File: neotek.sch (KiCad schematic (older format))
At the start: 18 parts, among them P1 USB_OTG, U1 STM32F103C4, U2 MIC5219-3.3, Y1 Crystal

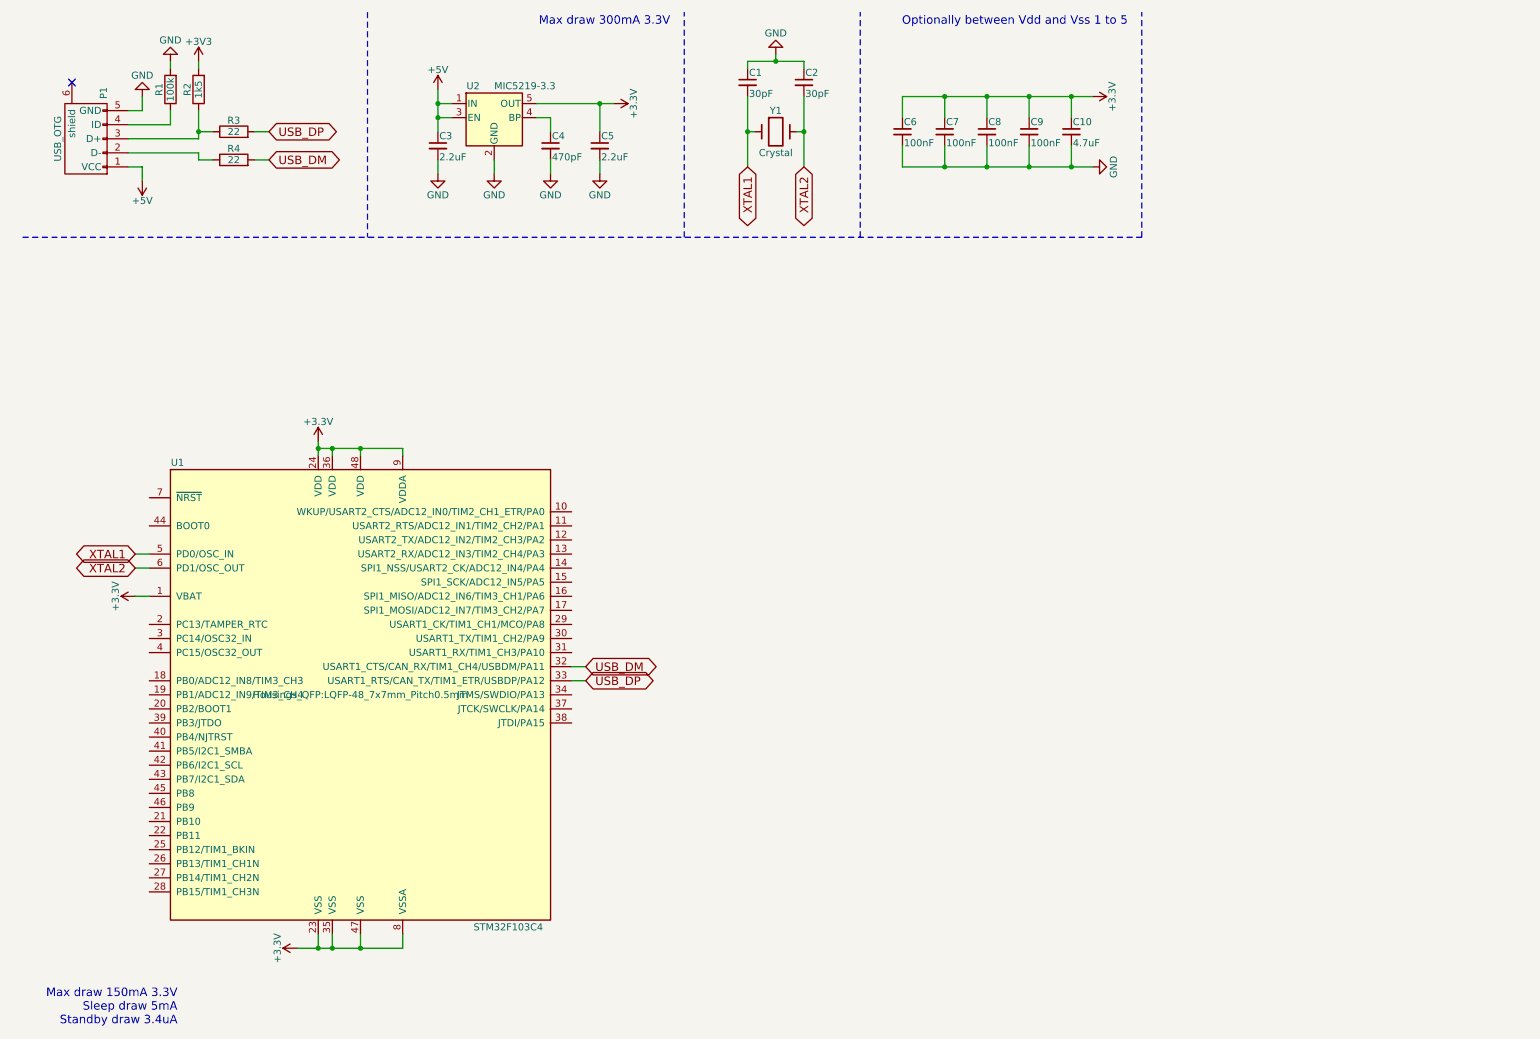
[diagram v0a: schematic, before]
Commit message: Added headers; made footprint & layout stub
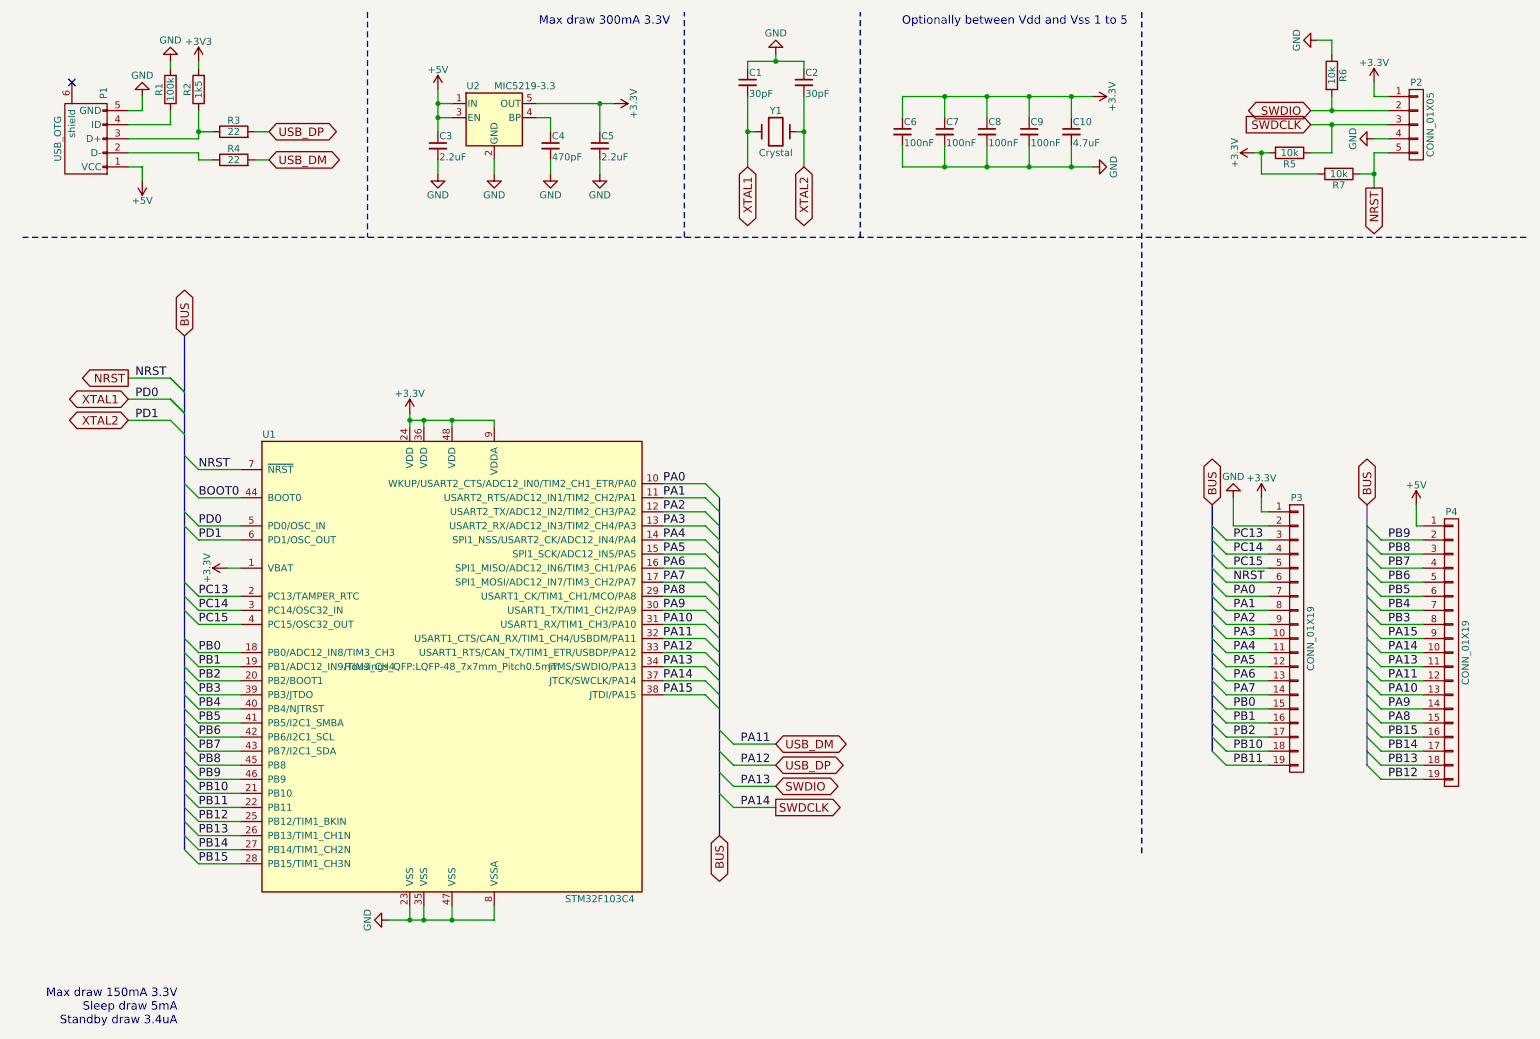
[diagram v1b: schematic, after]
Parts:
- added P2: CONN_01X05, Connectors_Hirose:Hirose_DF13-05P-1.25DS_05x1.25mm_Angled, symbol CONN_01X05
- added P3, P4: CONN_01X19, Pin_Headers:Pin_Header_Straight_1x19, symbol CONN_01X19
- added R5, R6, R7: 10k, Resistors_SMD:R_0603_HandSoldering, symbol R
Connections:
- net +3V3: now also P2.1 (P1), P3.1 (P1), R5.2, R7.2; no longer U1.23 (VSS), U1.35 (VSS), U1.47 (VSS), U1.8 (VSSA)
- net +5V: now also P4.1 (P1)
- net GND: now also U1.23 (VSS), U1.35 (VSS), U1.47 (VSS), U1.8 (VSSA), P2.4 (P4), P3.2 (P2), R6.1
- net USB_DM: now also P4.12 (P12)
- net PA0: now reaches U1.10 (WKUP/USART2_CTS/ADC12_IN0/TIM2_CH1_ETR/PA0)
- net PA0: now also P3.7 (P7)
- net PA1: now reaches U1.11 (USART2_RTS/ADC12_IN1/TIM2_CH2/PA1)
- net PA1: now also P3.8 (P8)
- net PA2: now reaches U1.12 (USART2_TX/ADC12_IN2/TIM2_CH3/PA2)
- net PA2: now also P3.9 (P9)
- net PA3: now reaches U1.13 (USART2_RX/ADC12_IN3/TIM2_CH4/PA3)
- net PA3: now also P3.10 (P10)
- net PA4: now reaches U1.14 (SPI1_NSS/USART2_CK/ADC12_IN4/PA4)
- net PA4: now also P3.11 (P11)
- net PA5: now reaches U1.15 (SPI1_SCK/ADC12_IN5/PA5)
- net PA5: now also P3.12 (P12)
- net PA6: now reaches U1.16 (SPI1_MISO/ADC12_IN6/TIM3_CH1/PA6)
- net PA6: now also P3.13 (P13)
- net PA7: now reaches U1.17 (SPI1_MOSI/ADC12_IN7/TIM3_CH2/PA7)
- net PA7: now also P3.14 (P14)
- net PB0: now reaches U1.18 (PB0/ADC12_IN8/TIM3_CH3)
- net PB0: now also P3.15 (P15)
- net PB1: now reaches U1.19 (PB1/ADC12_IN9/TIM3_CH4)
- net PB1: now also P3.16 (P16)
- net PC13: now reaches U1.2 (PC13/TAMPER_RTC)
- net PC13: now also P3.3 (P3)
- net PB2: now reaches U1.20 (PB2/BOOT1)
- net PB2: now also P3.17 (P17)
- net PB10: now reaches U1.21 (PB10)
- net PB10: now also P3.18 (P18)
- net PB11: now reaches U1.22 (PB11)
- net PB11: now also P3.19 (P19)
- net PB12: now reaches U1.25 (PB12/TIM1_BKIN)
- net PB12: now also P4.19 (P19)
- net PB13: now reaches U1.26 (PB13/TIM1_CH1N)
- net PB13: now also P4.18 (P18)
- net PB14: now reaches U1.27 (PB14/TIM1_CH2N)
- net PB14: now also P4.17 (P17)
- net PB15: now reaches U1.28 (PB15/TIM1_CH3N)
- net PB15: now also P4.16 (P16)
- net PA8: now reaches U1.29 (USART1_CK/TIM1_CH1/MCO/PA8)
- net PA8: now also P4.15 (P15)
- net PC14: now reaches U1.3 (PC14/OSC32_IN)
- net PC14: now also P3.4 (P4)
- net PA9: now reaches U1.30 (USART1_TX/TIM1_CH2/PA9)
- net PA9: now also P4.14 (P14)
- net PA10: now reaches U1.31 (USART1_RX/TIM1_CH3/PA10)
- net PA10: now also P4.13 (P13)
- net SWDIO: now reaches U1.34 (JTMS/SWDIO/PA13)
- net SWDIO: now also P2.2 (P2), P4.11 (P11), R6.2
- net SWDCLK: now reaches U1.37 (JTCK/SWCLK/PA14)
- net SWDCLK: now also P2.3 (P3), P4.10 (P10), R5.1
- net PA15: now reaches U1.38 (JTDI/PA15)
- net PA15: now also P4.9 (P9)
- net PB3: now reaches U1.39 (PB3/JTDO)
- net PB3: now also P4.8 (P8)
- net PC15: now reaches U1.4 (PC15/OSC32_OUT)
- net PC15: now also P3.5 (P5)
- net PB4: now reaches U1.40 (PB4/NJTRST)
- net PB4: now also P4.7 (P7)
- net PB5: now reaches U1.41 (PB5/I2C1_SMBA)
- net PB5: now also P4.6 (P6)
- net PB6: now reaches U1.42 (PB6/I2C1_SCL)
- net PB6: now also P4.5 (P5)
- net PB7: now reaches U1.43 (PB7/I2C1_SDA)
- net PB7: now also P4.4 (P4)
- net BOOT0: now reaches U1.44 (BOOT0)
- net PB8: now reaches U1.45 (PB8)
- net PB8: now also P4.3 (P3)
- net PB9: now reaches U1.46 (PB9)
- net PB9: now also P4.2 (P2)
- net NRST: now reaches U1.7 (~NRST)
- net NRST: now also P2.5 (P5), P3.6 (P6), R7.1
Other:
- moved on the sheet: U1

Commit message: wip
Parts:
- P1: footprint Connect:USB_Micro-B -> Connect:USB_Micro-B_10103594-0001LF
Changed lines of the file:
@@
 F 0 "P1" H 1275 1275 50  0000 C CNN
 F 1 "USB_OTG" H 950 1600 50  0000 C CNN
-F 2 "Connect:USB_Micro-B" V 900 1300 50  0001 C CNN
+F 2 "Connect:USB_Micro-B_10103594-0001LF" V 900 1300 50  0001 C CNN
 F 3 "" V 900 1300 50  0000 C CNN
 	1    950  1400
@@
 Connection ~ 3550 6950
 $Comp
-L +3.3V #PWR07
+L +3.3V #PWR06
 U 1 1 5A6E46B8
 P 3250 3350
-F 0 "#PWR07" H 3250 3200 50  0001 C CNN
+F 0 "#PWR06" H 3250 3200 50  0001 C CNN
 F 1 "+3.3V" H 3250 3490 50  0000 C CNN
 F 2 "" H 3250 3350 50  0000 C CNN
@@
 Connection ~ 3550 3400
 $Comp
-L +3.3V #PWR08
+L +3.3V #PWR07
 U 1 1 5A6E4886
 P 1950 4450
-F 0 "#PWR08" H 1950 4300 50  0001 C CNN
+F 0 "#PWR07" H 1950 4300 50  0001 C CNN
 F 1 "+3.3V" H 1950 4590 50  0000 C CNN
 F 2 "" H 1950 4450 50  0000 C CNN
@@
 $EndComp
 $Comp
-L +5V #PWR09
+L +5V #PWR08
 U 1 1 5A6E4C63
 P 3450 1050
-F 0 "#PWR09" H 3450 900 50  0001 C CNN
+F 0 "#PWR08" H 3450 900 50  0001 C CNN
 F 1 "+5V" H 3450 1190 50  0000 C CNN
 F 2 "" H 3450 1050 50  0000 C CNN
@@
 	3450 1150 3550 1150
 $Comp
-L GND #PWR010
+L GND #PWR09
 U 1 1 5A6E4D61
 P 3850 1650
-F 0 "#PWR010" H 3850 1400 50  0001 C CNN
+F 0 "#PWR09" H 3850 1400 50  0001 C CNN
 F 1 "GND" H 3850 1500 50  0000 C CNN
 F 2 "" H 3850 1650 50  0000 C CNN
@@
 $EndComp
 $Comp
-L GND #PWR011
+L GND #PWR010
 U 1 1 5A6E4E0C
 P 4250 1650
-F 0 "#PWR011" H 4250 1400 50  0001 C CNN
+F 0 "#PWR010" H 4250 1400 50  0001 C CNN
 F 1 "GND" H 4250 1500 50  0000 C CNN
 F 2 "" H 4250 1650 50  0000 C CNN
@@
 $EndComp
 $Comp
-L GND #PWR012
+L GND #PWR011
 U 1 1 5A6E50E3
 P 4600 1650
-F 0 "#PWR012" H 4600 1400 50  0001 C CNN
+F 0 "#PWR011" H 4600 1400 50  0001 C CNN
 F 1 "GND" H 4600 1500 50  0000 C CNN
 F 2 "" H 4600 1650 50  0000 C CNN
@@
 Connection ~ 3450 1250
 $Comp
-L GND #PWR013
+L GND #PWR012
 U 1 1 5A6E5BDB
 P 3450 1650
-F 0 "#PWR013" H 3450 1400 50  0001 C CNN
+F 0 "#PWR012" H 3450 1400 50  0001 C CNN
 F 1 "GND" H 3450 1500 50  0000 C CNN
 F 2 "" H 3450 1650 50  0000 C CNN
@@
 $EndComp
 $Comp
-L GND #PWR014
+L GND #PWR013
 U 1 1 5A6E6C90
 P 8100 1600
-F 0 "#PWR014" H 8100 1350 50  0001 C CNN
+F 0 "#PWR013" H 8100 1350 50  0001 C CNN
 F 1 "GND" H 8100 1450 50  0000 C CNN
 F 2 "" H 8100 1600 50  0000 C CNN
@@
 $EndComp
 $Comp
-L +3.3V #PWR015
+L +3.3V #PWR014
 U 1 1 5A6E6E8E
 P 4700 1150
-F 0 "#PWR015" H 4700 1000 50  0001 C CNN
+F 0 "#PWR014" H 4700 1000 50  0001 C CNN
 F 1 "+3.3V" H 4700 1290 50  0000 C CNN
 F 2 "" H 4700 1150 50  0000 C CNN
@@
 $EndComp
 $Comp
-L +3.3V #PWR016
+L +3.3V #PWR015
 U 1 1 5A6E6F17
 P 8100 1100
-F 0 "#PWR016" H 8100 950 50  0001 C CNN
+F 0 "#PWR015" H 8100 950 50  0001 C CNN
 F 1 "+3.3V" H 8100 1240 50  0000 C CNN
 F 2 "" H 8100 1100 50  0000 C CNN
@@
 	8450 500  8450 6500
 $Comp
-L +3.3V #PWR017
+L +3.3V #PWR016
 U 1 1 5A6F8D21
 P 10100 1000
-F 0 "#PWR017" H 10100 850 50  0001 C CNN
+F 0 "#PWR016" H 10100 850 50  0001 C CNN
 F 1 "+3.3V" H 10100 1140 50  0000 C CNN
 F 2 "" H 10100 1000 50  0000 C CNN
@@
 SWDIO
 $Comp
-L GND #PWR018
+L GND #PWR017
 U 1 1 5A6F91D4
 P 9700 700
-F 0 "#PWR018" H 9700 450 50  0001 C CNN
+F 0 "#PWR017" H 9700 450 50  0001 C CNN
 F 1 "GND" H 9700 550 50  0000 C CNN
 F 2 "" H 9700 700 50  0000 C CNN
@@
 Connection ~ 9800 1200
 $Comp
-L GND #PWR019
+L GND #PWR018
 U 1 1 5A6F96FC
 P 10100 1400
-F 0 "#PWR019" H 10100 1150 50  0001 C CNN
+F 0 "#PWR018" H 10100 1150 50  0001 C CNN
 F 1 "GND" H 10100 1250 50  0000 C CNN
 F 2 "" H 10100 1400 50  0000 C CNN
@@
 Connection ~ 9800 1300
 $Comp
-L +3.3V #PWR020
+L +3.3V #PWR019
 U 1 1 5A6F9C7A
 P 9250 1500
-F 0 "#PWR020" H 9250 1350 50  0001 C CNN
+F 0 "#PWR019" H 9250 1350 50  0001 C CNN
 F 1 "+3.3V" H 9250 1640 50  0000 C CNN
 F 2 "" H 9250 1500 50  0000 C CNN
@@
 NRST
 $Comp
-L +3.3V #PWR021
+L +3.3V #PWR020
 U 1 1 5A708845
 P 9300 3950
-F 0 "#PWR021" H 9300 3800 50  0001 C CNN
+F 0 "#PWR020" H 9300 3800 50  0001 C CNN
 F 1 "+3.3V" H 9300 4090 50  0000 C CNN
 F 2 "" H 9300 3950 50  0000 C CNN
@@
 $EndComp
 $Comp
-L GND #PWR022
+L GND #PWR021
 U 1 1 5A708A18
 P 9100 3950
-F 0 "#PWR022" H 9100 3700 50  0001 C CNN
+F 0 "#PWR021" H 9100 3700 50  0001 C CNN
 F 1 "GND" H 9100 3800 50  0000 C CNN
 F 2 "" H 9100 3950 50  0000 C CNN
@@
 $EndComp
 $Comp
-L +5V #PWR023
+L +5V #PWR022
 U 1 1 5A708B9F
 P 10400 4000
-F 0 "#PWR023" H 10400 3850 50  0001 C CNN
+F 0 "#PWR022" H 10400 3850 50  0001 C CNN
 F 1 "+5V" H 10400 4140 50  0000 C CNN
 F 2 "" H 10400 4000 50  0000 C CNN
@@
 	10400 4150 10400 4000
 $Comp
-L GND #PWR?
+L GND #PWR023
 U 1 1 5A70F79F
 P 3100 6950
-F 0 "#PWR?" H 3100 6700 50  0001 C CNN
+F 0 "#PWR023" H 3100 6700 50  0001 C CNN
 F 1 "GND" H 3100 6800 50  0000 C CNN
 F 2 "" H 3100 6950 50  0000 C CNN
